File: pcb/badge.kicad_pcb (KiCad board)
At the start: 2 copper layers, 12 parts, among them IC1 ATTINY48-A, IC2 AAT3681A, P1 CONN_02X07, P2 CONN_01X06, P3 CONN_01X02, P4 USB_OTG

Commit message: started work on the hat edition
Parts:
- removed C1: C, netl:SMD_0603
- removed D1: D, netl:SMD_0603
- removed D2: LED, netl:SMD_0603
- removed IC1: ATTINY48-A, Housings_QFP:TQFP-32_7x7mm_Pitch0.8mm
- removed IC2: AAT3681A, netl:SC70JW-8
- removed P1: CONN_02X07, netl:8x2_backlight
- removed P2: CONN_01X06, Connect:PINHEAD1-6
- removed P3: CONN_01X02, Pin_Headers:Pin_Header_Straight_1x02
- removed P4: USB_OTG, Connect:USB_Micro-B
- removed R1, R2: R, netl:SMD_0603
- removed R3: 0R, netl:SMD_0603
- added C101: C, netl:SMD_0603, F.Cu at (166.0, 144.0)
- added C102: C, netl:SMD_0603, F.Cu at (173.0, 145.0)
- added C103: C, netl:SMD_0603, F.Cu at (169.0, 130.0)
- added C104: C, netl:SMD_0603, F.Cu at (135.2, 122.8)
- added C105: 100n, netl:SMD_0603, F.Cu at (148.8, 125.0)
- added D101: LED, netl:SMD_0603, F.Cu at (180.0, 121.0)
- added IC101: ATMEGA8-AI, Housings_QFP:TQFP-32_7x7mm_Pitch0.8mm, F.Cu at (172.0, 123.0)
- added IC102: AAT3681A, netl:SC70JW-8, F.Cu at (129.5, 118.8)
- added P101: CONN_02X03, Pin_Headers:Pin_Header_Straight_2x03, F.Cu at (181.0, 117.0)
- added P102: CONN_01X02, Pin_Headers:Pin_Header_Straight_1x02, F.Cu at (104.0, 119.0)
- added P103: USB_OTG, Connect:USB_Micro-B, F.Cu at (137.0, 106.0)
- added P104: CONNECTOR, netl:1Pin_small, F.Cu at (154.0, 117.0)
- added P105: CONNECTOR, netl:1Pin_small, F.Cu at (160.0, 117.0)
- added P106: CONNECTOR, netl:1Pin_small, F.Cu at (156.0, 117.0)
- added P107: CONNECTOR, netl:1Pin_small, F.Cu at (162.0, 117.0)
- added P108: CONNECTOR, netl:1Pin_small, F.Cu at (164.0, 117.0)
- added P109: CONNECTOR, netl:1Pin_small, F.Cu at (158.0, 117.0)
- added Q101: FT230XS-R, Housings_SSOP:SSOP-16_5.3x6.2mm_Pitch0.65mm, F.Cu at (142.0, 123.0)
- added Q102: NPN, TO_SOT_Packages_SMD:SOT-323, F.Cu at (153.0, 122.0)
- added R101: 10k, netl:SMD_0603, F.Cu at (164.0, 123.0)
- added R102: R, netl:SMD_0603, F.Cu at (182.0, 132.0)
- added R103: R, netl:SMD_0603, F.Cu at (180.0, 123.0)
- added R105: R, netl:SMD_0603, F.Cu at (129.2, 116.5)
- added R106: R, netl:SMD_0603, F.Cu at (148.8, 126.8)
- added R107: R, netl:SMD_0603, F.Cu at (148.0, 122.0)
- added R108: R, netl:SMD_0603, F.Cu at (150.0, 122.0)
- added SW101: SW_PUSH, Buttons_Switches_SMD:SW_SPST_EVQPE1, F.Cu at (183.0, 126.0)
- added Y101: Crystal, Crystals:Crystal_HC49-U_Vertical, F.Cu at (175.0, 131.0)
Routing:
- net VDD: track 95.5 -> 0.00 mm
- net ~RESET: track 17.4 -> 0.00 mm
- net DB7: track 16.2 -> 0.00 mm
- net DB5: track 14.6 -> 0.00 mm
- net RS: track 14.4 -> 0.00 mm
- net 3V3: track 0.00 -> 13.6 mm
- net E: track 13.1 -> 0.00 mm
- net DB6: track 11.7 -> 0.00 mm
- net V_USB: track 9.02 -> 20.6 mm
- net DB4: track 11.3 -> 0.00 mm
- net SCK: track 10.7 -> 0.00 mm
- net R/W: track 9.83 -> 0.00 mm
- net MOSI: track 8.86 -> 0.00 mm
- net MISO: track 8.76 -> 0.00 mm
- net Net-(Q101-Pad4): track 0.00 -> 7.42 mm
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- removed copper zone on F.Cu, net VSS
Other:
- board outline added: 77 x 21 mm

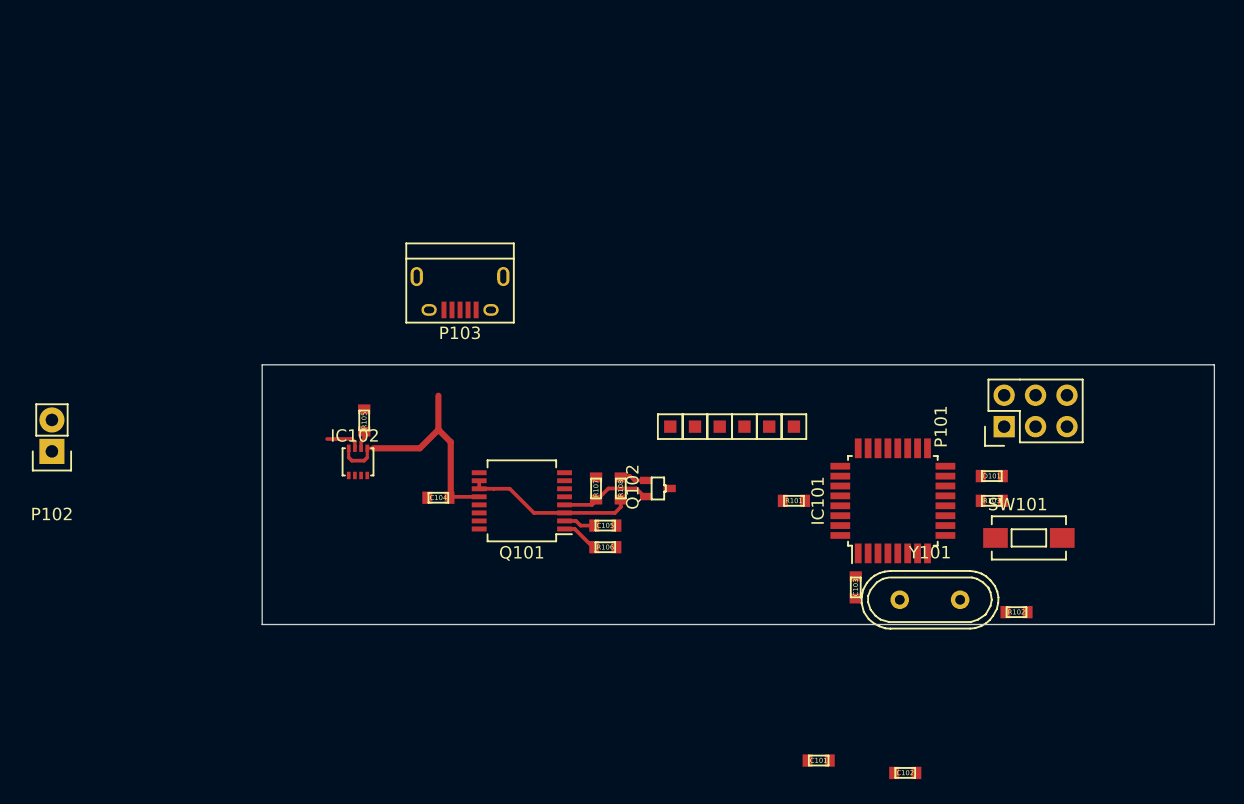
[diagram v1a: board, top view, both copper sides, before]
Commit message: now just a plain serial programmer with a lipo charger
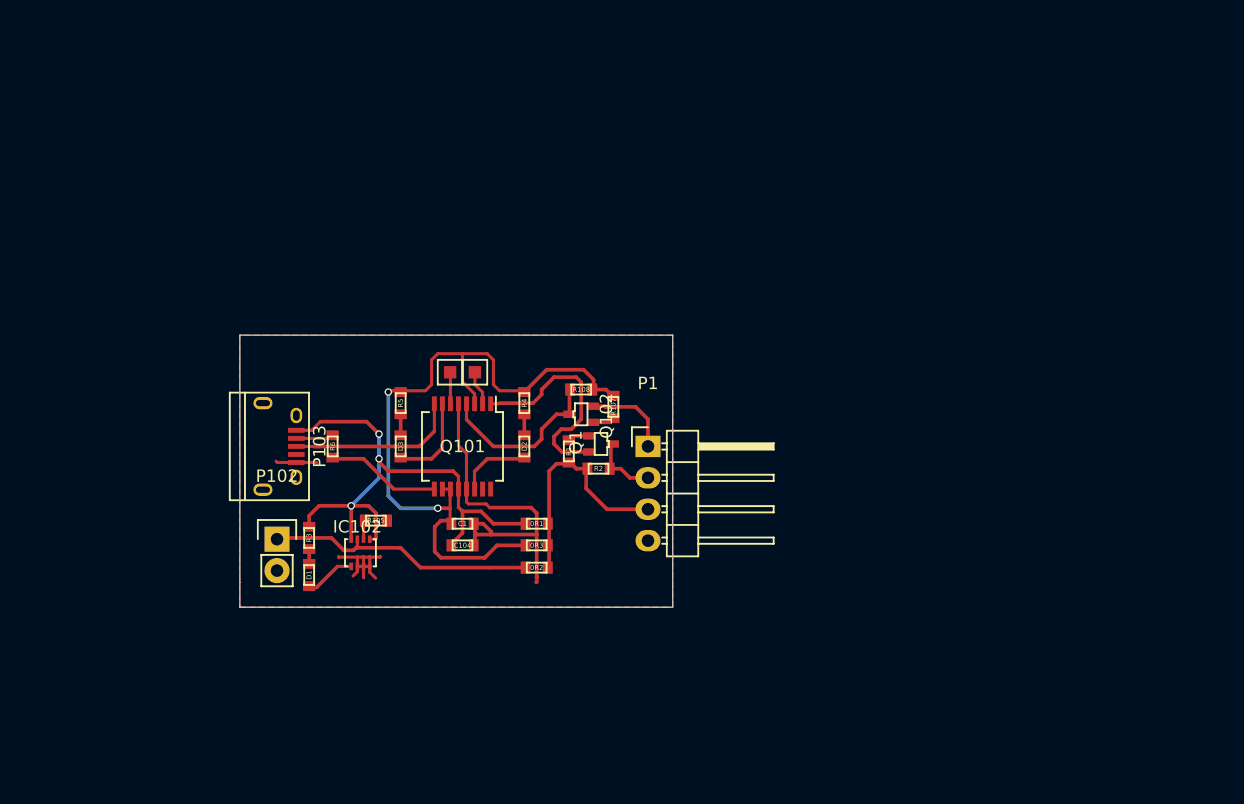
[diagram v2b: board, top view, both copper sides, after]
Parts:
- removed C101, C102, C103: C, netl:SMD_0603
- removed C105: 100n, netl:SMD_0603
- removed D101: LED, netl:SMD_0603
- removed IC101: ATMEGA8-AI, Housings_QFP:TQFP-32_7x7mm_Pitch0.8mm
- removed P101: CONN_02X03, Pin_Headers:Pin_Header_Straight_2x03
- removed P104, P105, P106, P107, P108, P109: CONNECTOR, netl:1Pin_small
- removed R101: 10k, netl:SMD_0603
- removed R102, R103, R106: R, netl:SMD_0603
- removed SW101: SW_PUSH, Buttons_Switches_SMD:SW_SPST_EVQPE1
- removed Y101: Crystal, Crystals:Crystal_HC49-U_Vertical
- added 0R1: R, netl:SMD_0603, F.Cu at (143.2, 124.8)
- added 0R2: R, netl:SMD_0603, F.Cu at (143.2, 128.4)
- added 0R3: R, netl:SMD_0603, F.Cu at (143.2, 126.6)
- added C1: 10u, netl:SMD_0603, F.Cu at (137.2, 124.8)
- added D1: LED, netl:SMD_0603, F.Cu at (124.8, 129.0)
- added D2: LED, netl:SMD_0603, F.Cu at (142.2, 118.6)
- added D3: LED, netl:SMD_0603, F.Cu at (132.2, 118.6)
- added P1: CONN_01X04, Pin_Headers:Pin_Header_Angled_1x04, F.Cu at (152.2, 118.6)
- added P2: CONNECTOR, netl:1Pin_small, F.Cu at (138.2, 112.6)
- added P3: CONNECTOR, netl:1Pin_small, F.Cu at (136.2, 112.6)
- added Q1: NPN, TO_SOT_Packages_SMD:SOT-323, F.Cu at (148.4, 118.4)
- added R1: R, netl:SMD_0603, F.Cu at (145.8, 119.0)
- added R2: R, netl:SMD_0603, F.Cu at (148.2, 120.4)
- added R3: R, netl:SMD_0603, F.Cu at (124.8, 126.0)
- added R4: R, netl:SMD_0603, F.Cu at (142.2, 115.1)
- added R5: R, netl:SMD_0603, F.Cu at (132.2, 115.1)
- added R6: 0R, netl:SMD_0603, F.Cu at (126.7, 118.6)
- C104: value C -> 10u
- moved P102 19.5 mm to (122.2, 126.1), turned to 0 degrees
- moved P103 19.4 mm to (122.2, 118.6), turned to 270 degrees
- moved Q102 8.63 mm to (146.8, 116.0), turned to 270 degrees
- moved R108 8.62 mm to (146.8, 114.0), turned to 180 degrees
- moved R105 8.16 mm to (130.2, 124.6), turned to 0 degrees
- moved IC102 7.35 mm to (129.7, 126.1)
- moved R107 6.75 mm to (149.4, 115.4)
- moved Q101 6.51 mm to (137.2, 118.6), turned to 270 degrees
- moved C104 4.32 mm to (137.2, 126.6), turned to 0 degrees
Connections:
- P103 pad 2: D- -> Net-(P103-Pad2)
- P103 pad 4: (no net) -> Net-(P103-Pad4)
- Q101 pad 14: (no net) -> Net-(D2-Pad1)
- Q101 pad 15: (no net) -> Net-(Q101-Pad15)
- Q101 pad 16: (no net) -> Net-(Q101-Pad16)
- Q101 pad 6: (no net) -> Net-(P3-Pad1)
- Q101 pad 7: (no net) -> Net-(D3-Pad1)
- Q102 pad 2: Net-(Q101-Pad4) -> AVR_TX
- Q102 pad 3: AVR_TX -> Net-(Q101-Pad4)
- R107 pad 1: Net-(Q101-Pad4) -> Net-(Q102-Pad1)
- R107 pad 2: GND -> 3V3
- R108 pad 2: Net-(Q102-Pad1) -> Net-(Q101-Pad4)
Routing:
- net 3V3: track 13.6 -> 57.9 mm, vias 0 -> 2
- net GND: track 0.00 -> 42.0 mm
- net V_USB: track 20.6 -> 44.8 mm, vias 0 -> 3
- net VBat: track 2.85 -> 21.9 mm
- net AVR_VCC: track 0.00 -> 18.5 mm
- net Net-(Q1-Pad2): track 2.91 -> 18.1 mm
- net D+: track 0.00 -> 14.4 mm
- net D-: track 0.00 -> 9.24 mm
- net Net-(D3-Pad1): track 0.00 -> 7.31 mm
- net AVR_TX: track 0.00 -> 7.09 mm
- net Net-(Q101-Pad4): track 7.42 -> 14.1 mm
- net Net-(D2-Pad1): track 0.00 -> 5.87 mm
- net AVR_RX: track 0.00 -> 5.37 mm
- net chrg: track 0.00 -> 4.10 mm
- net Net-(P103-Pad2): track 0.00 -> 3.08 mm
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- added copper zone on F.Cu, net GND
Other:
- board size 77 x 21 mm -> 35 x 22 mm
